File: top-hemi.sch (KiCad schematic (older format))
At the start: 35 parts, among them J1 USB_B_Micro, J2 TC2030_NL, J3 FFC_0.5mm, J4 Conn_01x02, J5 Conn_01x02, U1 CP2102N, U4 ATmega328P-MU, U5 ADXL335, Y1 16MHz

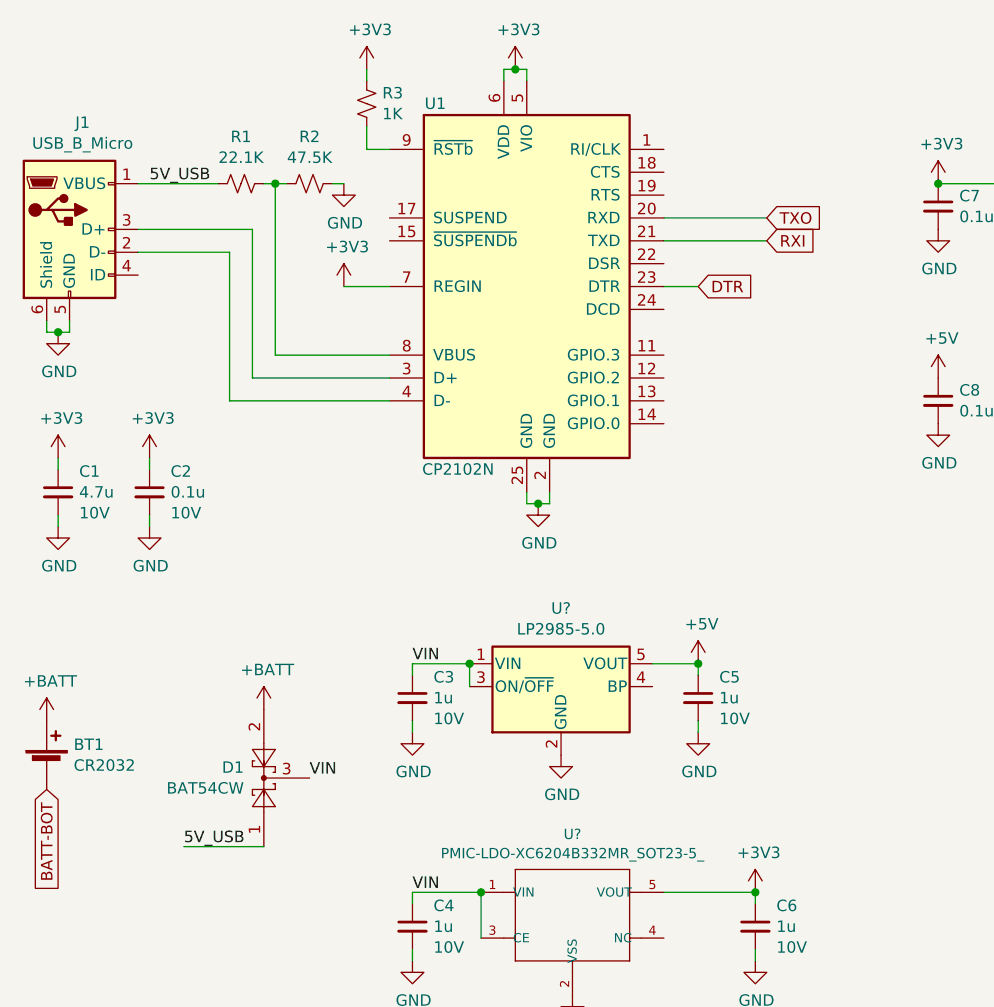
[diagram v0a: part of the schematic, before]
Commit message: Removed serial converter
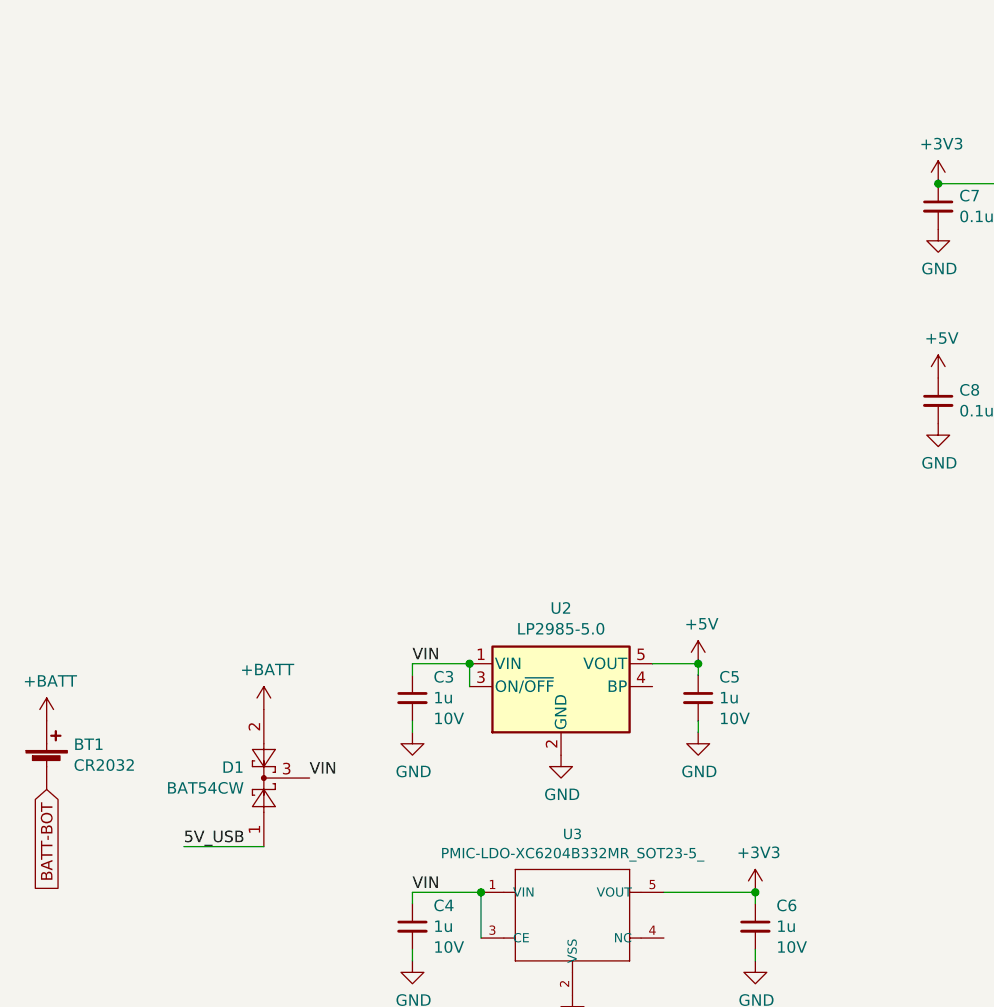
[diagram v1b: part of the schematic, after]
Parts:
- removed C1: 4.7u, Capacitor_SMD:C_0402_1005Metric, symbol Device:C_Small
- removed C2: 0.1u, Capacitor_SMD:C_0402_1005Metric, symbol Device:C_Small
- removed J1: USB_B_Micro, symbol Connector:USB_B_Micro
- removed R1: 22.1K, symbol Device:R_Small_US
- removed R2: 47.5K, symbol Device:R_Small_US
- removed R3: 1K, symbol Device:R_Small_US
- removed U1: CP2102N, Package_DFN_QFN:QFN-24-1EP_4x4mm_P0.5mm_EP2.6x2.6mm, symbol Interface_USB:CP2102N-A01-GQFN24
- gave numbers to parts that had none: 2

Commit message: Refactored schematic, placed components, no wiring
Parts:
- removed BT1: CR2032, Battery:BatteryHolder_Keystone_3034_1x20mm, symbol Device:Battery_Cell
- removed C10, C11, C12, C13, C7, C8, C9: 0.1u, Capacitor_SMD:C_0402_1005Metric, symbol Device:C_Small
- removed C3, C4, C5, C6: 1u, Capacitor_SMD:C_0603_1608Metric, symbol Device:C_Small
- removed D1: BAT54CW, Package_TO_SOT_SMD:SOT-323_SC-70, symbol Diode:BAT54CW
- removed D2, D3: NeoPixel_THT, LED_THT:LED_D5.0mm-4_RGB_Wide_Pins, symbol LED:NeoPixel_THT
- removed J2: TC2030_NL, symbol Connector_Generic:Conn_01x06
- removed J3: FFC_0.5mm, symbol Connector_Generic:Conn_01x06
- removed J4, J5: Conn_01x02, symbol Connector_Generic:Conn_01x02
- removed R4, R7: 4K7, symbol Device:R_Small_US
- removed R5: 470R, symbol Device:R_Small_US
- removed R6: 10K, symbol Device:R_Small_US
- removed U2: LP2985-5.0, Package_TO_SOT_SMD:SOT-23-5, symbol Regulator_Linear:LP2985-5.0
- removed U3: PMIC-LDO-XC6204B332MR_SOT23-5_, symbol OPL_Integrated_Circuit:PMIC-LDO-XC6204B332MR_SOT23-5_
- removed U4: ATmega328P-MU, Package_DFN_QFN:QFN-32-1EP_5x5mm_P0.5mm_EP3.1x3.1mm, symbol MCU_Microchip_ATmega:ATmega328P-MU
- removed U5: ADXL335, LFCSP-16, symbol SparkfunSensors:ADXL335
- removed Y1: 16MHz, symbol Device:Resonator_Small
